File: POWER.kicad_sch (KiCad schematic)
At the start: 18 parts, among them J100 VCC INPUT, J101 SWITCH ON/OFF, J102 JUMPER ON/OFF TEST, J103 FAN VOLTAGE, Q100 WST4045, U100 LM2596S-5, U101 AMS1117-3.3

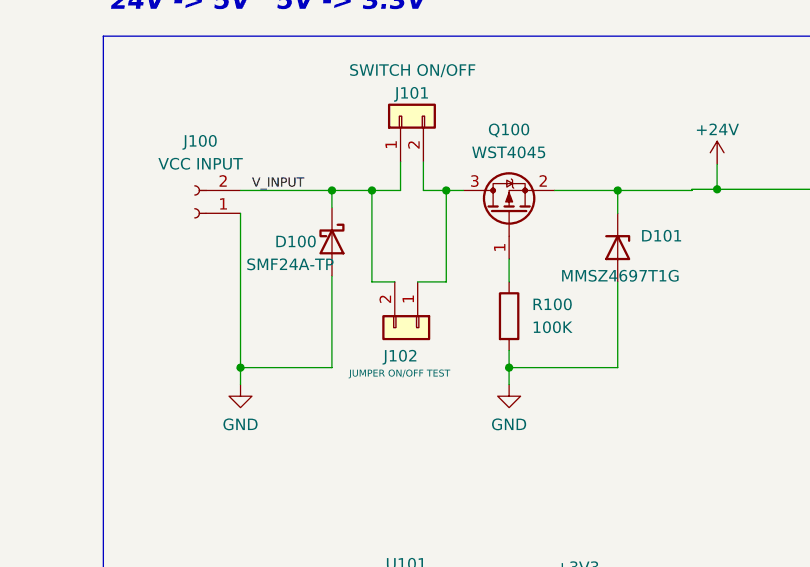
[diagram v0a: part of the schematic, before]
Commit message: added component labels
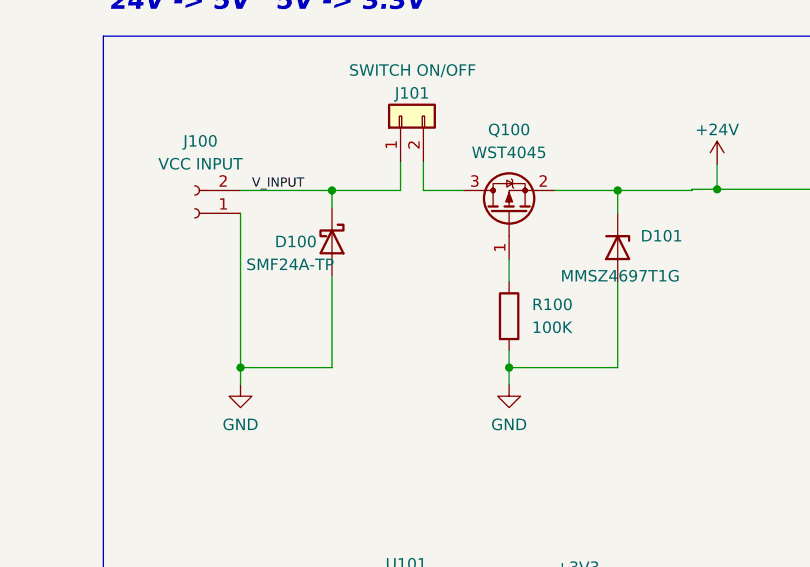
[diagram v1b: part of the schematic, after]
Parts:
- removed J102: JUMPER ON/OFF TEST, Connector_PinHeader_2.54mm:PinHeader_1x02_P2.54mm_Vertical, symbol Connector_Generic:Conn_01x02
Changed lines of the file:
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@@
 (kicad_sch (version 20211123) (generator eeschema)
   (paper "A4")
-  (junction (at 84.455 72.771) (diameter 0) (color 0 0 0 0)
-  )
   (junction (at 173.482 77.724) (diameter 0) (color 0 0 0 0)
   )
@@
   (junction (at 200.787 77.724) (diameter 0) (color 0 0 0 0)
   )
-  (junction (at 76.2 72.771) (diameter 0) (color 0 0 0 0)
-  )
   (junction (at 194.437 77.724) (diameter 0) (color 0 0 0 0)
   )
@@
     (stroke (width 0) (type default) (color 0 0 0 0))
   )
-  (wire (pts (xy 76.2 72.771) (xy 71.755 72.771))
+  (wire (pts (xy 71.755 72.771) (xy 79.375 72.771))
     (stroke (width 0) (type default) (color 0 0 0 0))
   )
@@
     (stroke (width 0) (type default) (color 0 0 0 0))
   )
-  (wire (pts (xy 79.375 72.771) (xy 76.2 72.771))
-    (stroke (width 0) (type default) (color 0 0 0 0))
-  )
   (wire (pts (xy 143.637 92.329) (xy 156.337 92.329))
     (stroke (width 0) (type default) (color 0 0 0 0))
@@
     (stroke (width 0) (type default) (color 0 0 0 0))
   )
-  (wire (pts (xy 76.2 82.931) (xy 76.2 72.771))
-    (stroke (width 0) (type default) (color 0 0 0 0))
-  )
   (wire (pts (xy 132.842 72.644) (xy 143.637 72.644))
     (stroke (width 0) (type default) (color 0 0 0 0))
@@
     (stroke (width 0) (type default) (color 0 0 0 0))
   )
-  (wire (pts (xy 78.74 82.931) (xy 76.2 82.931))
-    (stroke (width 0) (type default) (color 0 0 0 0))
-  )
   (wire (pts (xy 156.337 82.804) (xy 156.337 92.329))
     (stroke (width 0) (type default) (color 0 0 0 0))
@@
     (stroke (width 0) (type default) (color 0 0 0 0))
   )
-  (wire (pts (xy 84.455 82.931) (xy 84.455 72.771))
-    (stroke (width 0) (type default) (color 0 0 0 0))
-  )
   (wire (pts (xy 173.482 92.329) (xy 156.337 92.329))
     (stroke (width 0) (type default) (color 0 0 0 0))
@@
     (stroke (width 0) (type default) (color 0 0 0 0))
   )
-  (wire (pts (xy 84.455 72.771) (xy 86.36 72.771))
-    (stroke (width 0) (type default) (color 0 0 0 0))
-  )
   (wire (pts (xy 67.945 173.736) (xy 67.945 173.101))
     (stroke (width 0) (type default) (color 0 0 0 0))
@@
     (stroke (width 0) (type default) (color 0 0 0 0))
   )
-  (wire (pts (xy 81.915 72.771) (xy 84.455 72.771))
+  (wire (pts (xy 81.915 72.771) (xy 86.36 72.771))
     (stroke (width 0) (type default) (color 0 0 0 0))
   )
@@
   )
   (wire (pts (xy 67.31 131.826) (xy 67.31 133.096))
-    (stroke (width 0) (type default) (color 0 0 0 0))
-  )
-  (wire (pts (xy 81.28 82.931) (xy 84.455 82.931))
     (stroke (width 0) (type default) (color 0 0 0 0))
   )
@@
     (pin "1")
   )
-  (symbol (lib_id "Connector_Generic:Conn_01x02") (at 81.28 88.011 270) (unit 1)
-    (in_bom yes) (on_board yes)
-    (property "Reference" "J102" (id 0) (at 77.47 91.186 90)
-      (effects (font (size 1.27 1.27)) (justify left))
-    )
-    (property "Value" "JUMPER ON/OFF TEST" (id 1) (at 73.66 93.091 90)
-      (effects (font (size 0.762 0.762)) (justify left))
-    )
-    (property "Footprint" "Connector_PinHeader_2.54mm:PinHeader_1x02_P2.54mm_Vertical" (id 2) (at 81.28 88.011 0)
-      (effects (font (size 1.27 1.27)) hide)
-    )
-    (property "Datasheet" "~" (id 3) (at 81.28 88.011 0)
-      (effects (font (size 1.27 1.27)) hide)
-    )
-    (pin "1")
-    (pin "2")
-  )
   (symbol (lib_id "power:GND") (at 67.31 133.096 0) (unit 1)

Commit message: added BOM, Gerber and modified a few footprints
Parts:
- added TP100, TP101, TP102, TP103, TP104: TestPoint, TestPoint:TestPoint_Pad_D2.0mm, symbol Connector:TestPoint
- C100: value 100u -> 330u; LCSC (none) -> C239324
- C101: footprint Capacitor_SMD:C_Elec_8x10.2 -> Capacitor_SMD:CP_Elec_10x10.5; LCSC (none) -> C2886113
- C102, C103: LCSC C13585 -> C15850
- D100: LCSC (none) -> C545276
- D101: LCSC (none) -> C48870
- D102: LCSC (none) -> C8678
- D103: LCSC (none) -> C72043
- L100: LCSC (none) -> C2929504
- Q100: LCSC (none) -> C719073
- R100: LCSC (none) -> C17900
- R101: LCSC (none) -> C21190
- U100: LCSC (none) -> C10002
- U101: LCSC C347222 -> C6186
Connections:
- net +3V3: now also TP102.1
- net +5V: now also TP101.1
- net GND: now also TP103.1, TP104.1; no longer D101.2 (A)
- net V_INPUT: now also TP100.1
- net at Q100.1 (G), R100.1: now also D101.2 (A)
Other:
- moved on the sheet: D101
